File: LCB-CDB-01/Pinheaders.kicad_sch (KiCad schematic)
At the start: 4 parts, among them J60 Conn_02x30_Row_Letter_Last, J61 Conn_02x30_Row_Letter_Last, J62 Conn_02x30_Row_Letter_Last, J63 Conn_02x30_Row_Letter_Last

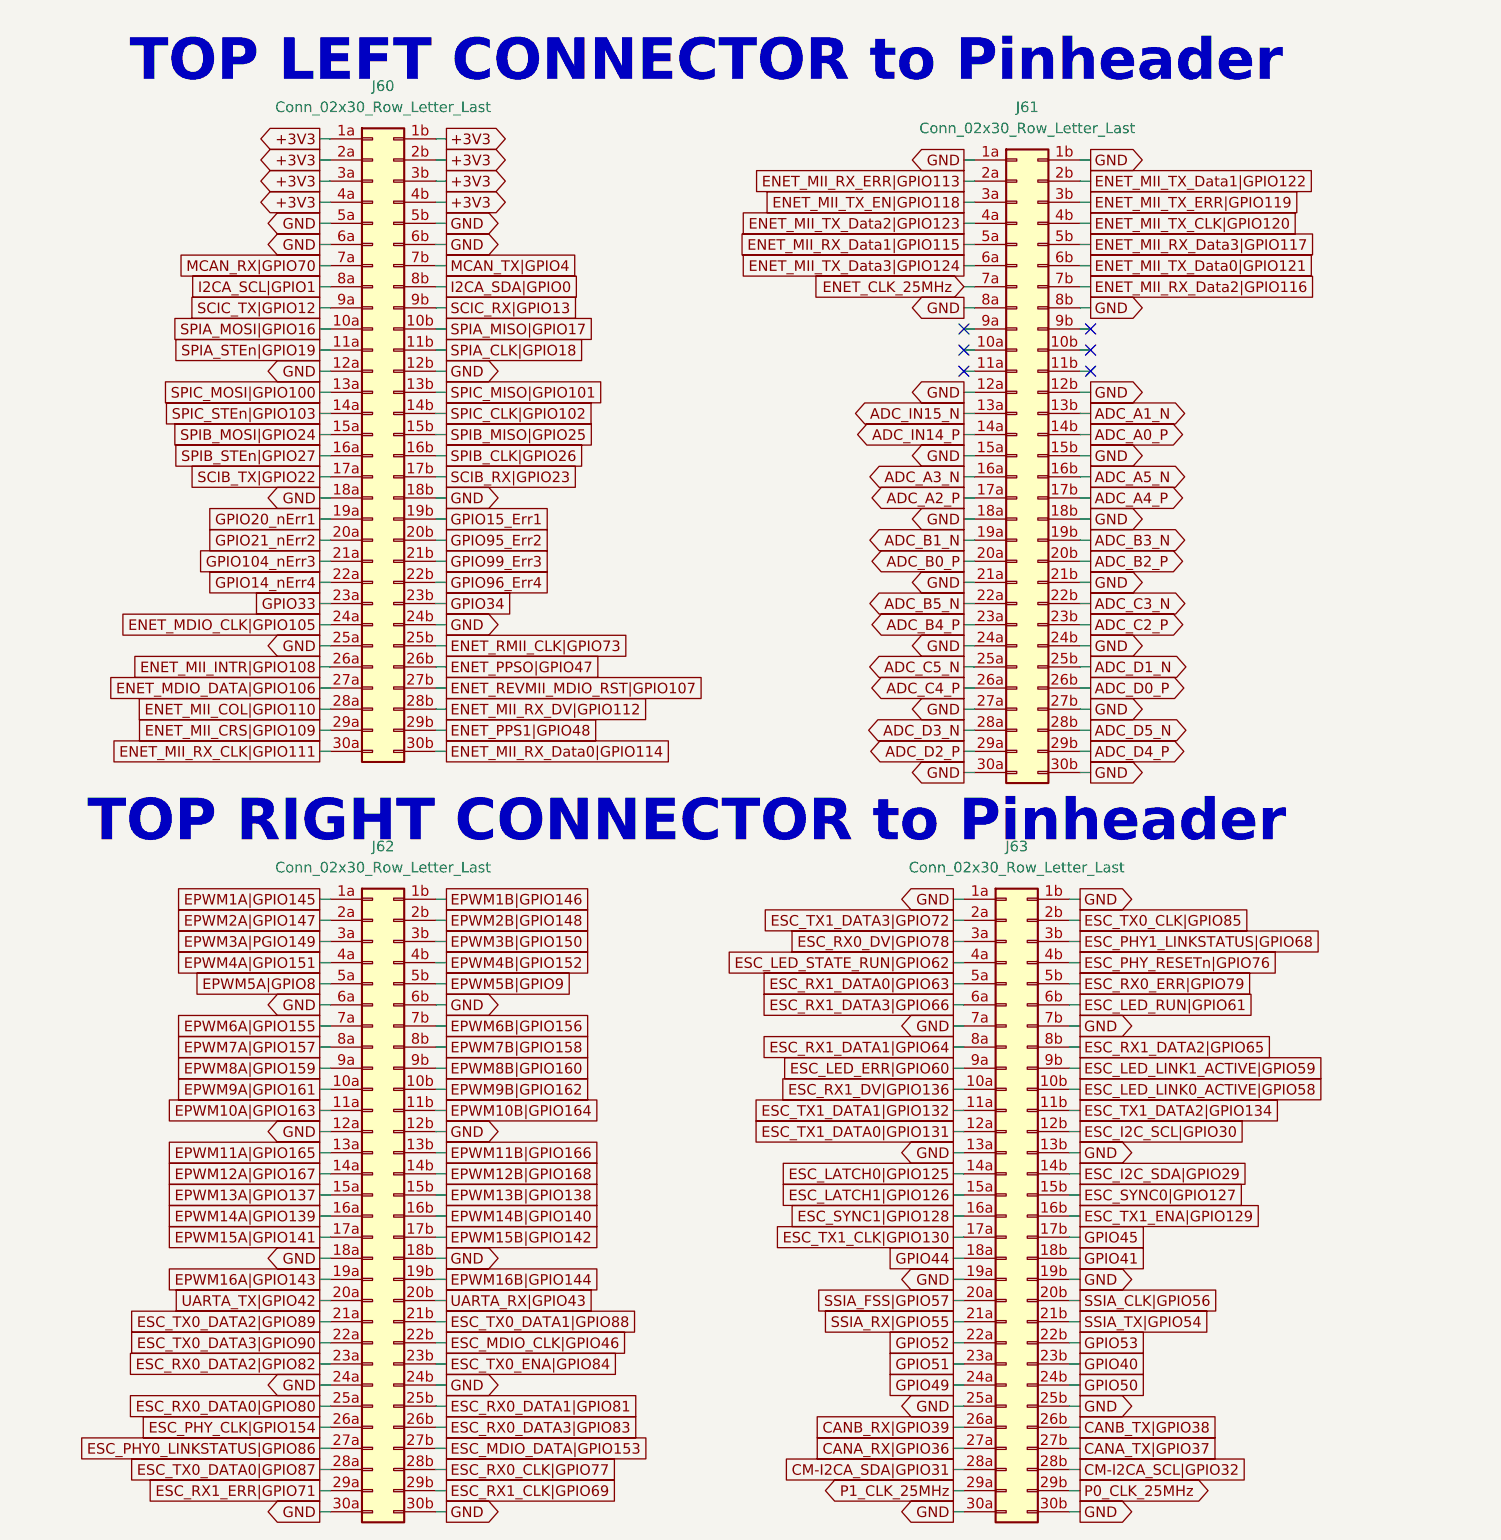
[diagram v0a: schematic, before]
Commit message: update some Rs and Cs names and values, as they can be separate values in KiCad7
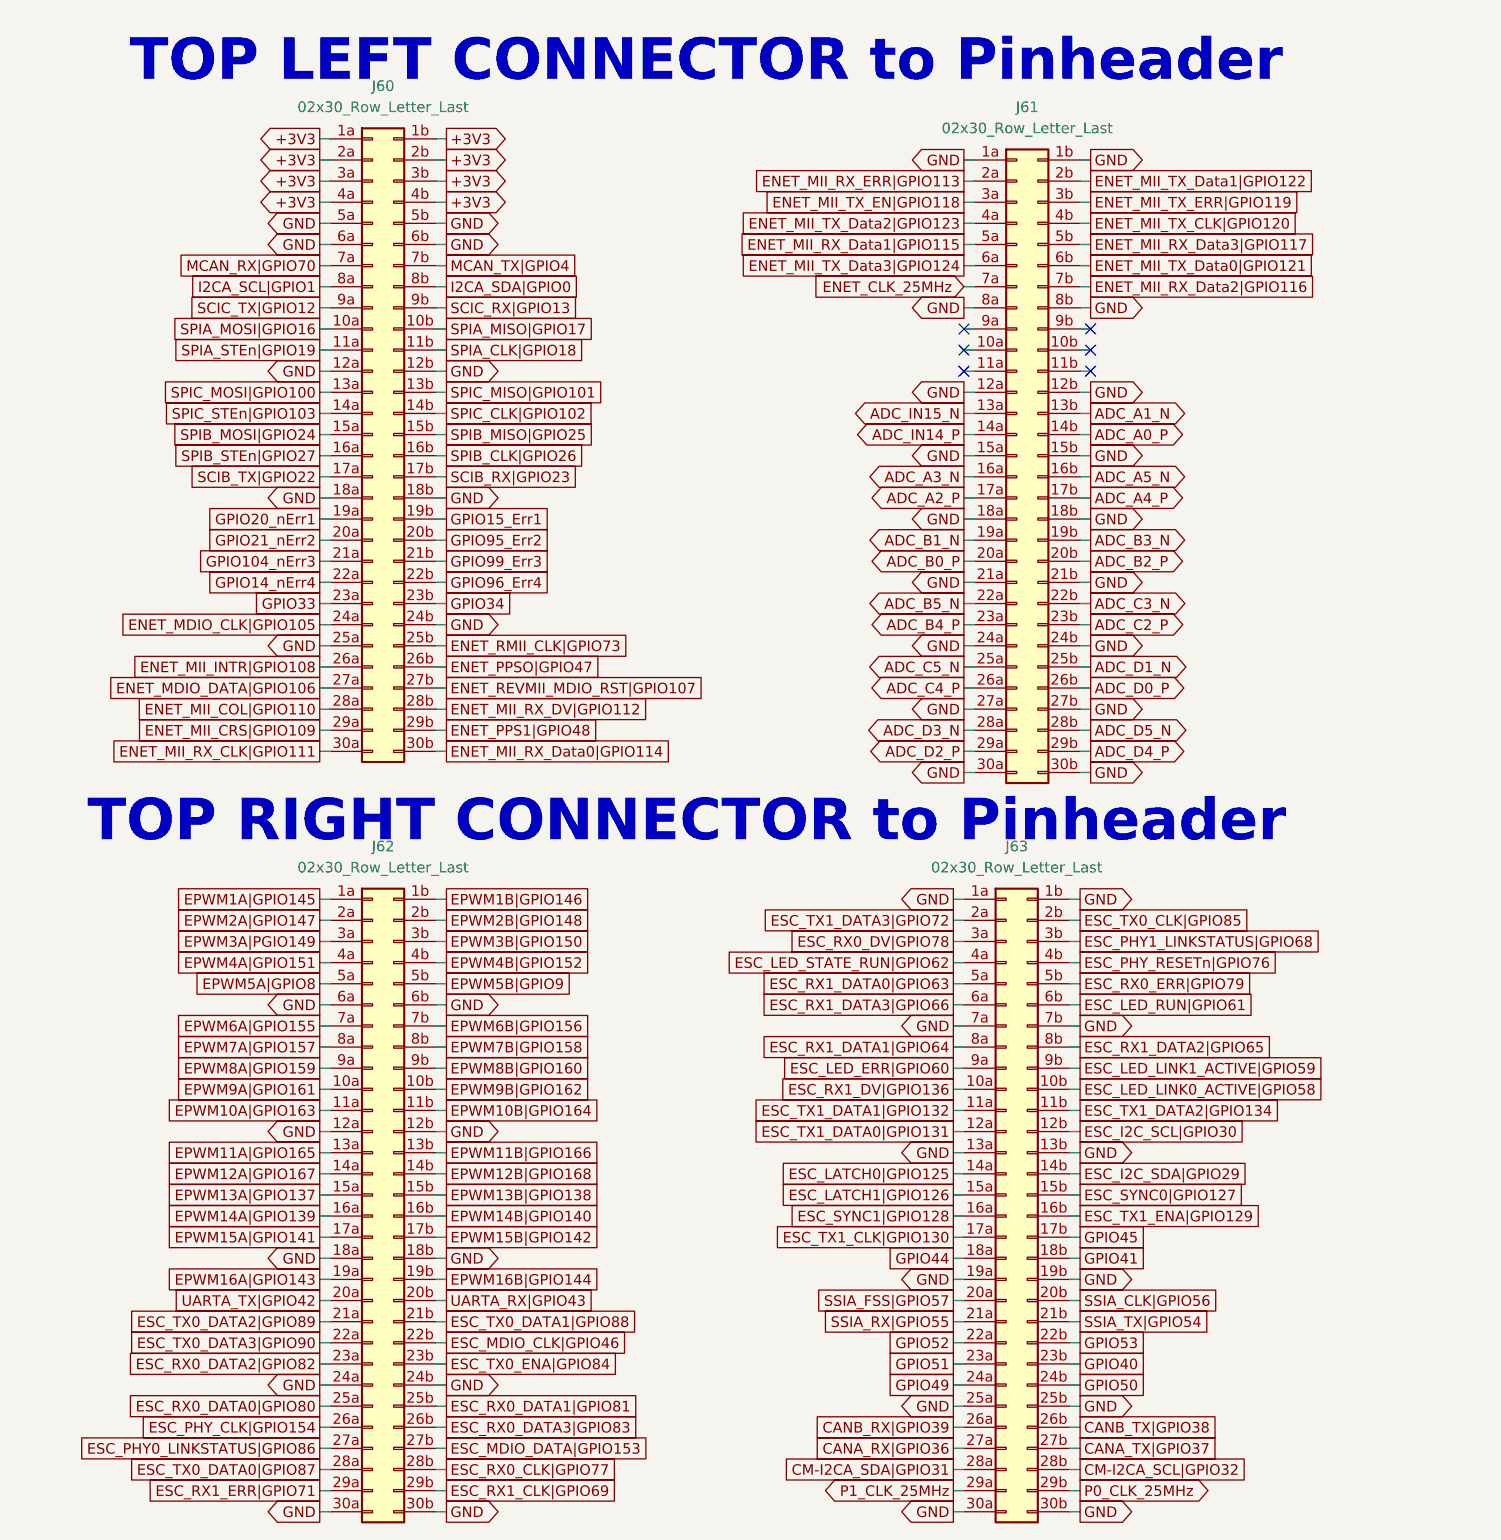
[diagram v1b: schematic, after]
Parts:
- J60, J61, J62, J63: value Conn_02x30_Row_Letter_Last -> 02x30_Row_Letter_Last
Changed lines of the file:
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@@
       (effects (font (size 1.27 1.27)))
     )
-    (property "Value" "Conn_02x30_Row_Letter_Last" (at 50.8 22.86 0)
+    (property "Value" "02x30_Row_Letter_Last" (at 50.8 22.86 0)
       (effects (font (size 1.27 1.27)))
     )
@@
       (effects (font (size 1.27 1.27)))
     )
-    (property "Value" "Conn_02x30_Row_Letter_Last" (at 50.8 114.3 0)
+    (property "Value" "02x30_Row_Letter_Last" (at 50.8 114.3 0)
       (effects (font (size 1.27 1.27)))
     )
@@
       (effects (font (size 1.27 1.27)))
     )
-    (property "Value" "Conn_02x30_Row_Letter_Last" (at 128.27 25.4 0)
+    (property "Value" "02x30_Row_Letter_Last" (at 128.27 25.4 0)
       (effects (font (size 1.27 1.27)))
     )
@@
       (effects (font (size 1.27 1.27)))
     )
-    (property "Value" "Conn_02x30_Row_Letter_Last" (at 127 114.3 0)
-      (effects (font (size 1.27 1.27)))
-    )
+    (property "Value" "02x30_Row_Letter_Last" (at 127 114.3 0)
+      (effects (font (size 1.27 1.27)))
+    )

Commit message: bump version to 1.1.0
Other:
- title: LCB-CBD-001: Dock -> LCB-CBD-01: Dock
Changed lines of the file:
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@@
   (paper "A4")
   (title_block
-    (title "LCB-CBD-001: Dock")
-    (date "2022-08-12")
-    (rev "0.1")
+    (title "LCB-CBD-01: Dock")
+    (date "2023-04-13")
+    (rev "1.1.0")
     (company "PADERBORN UNIVERSITY DEPARTMENT OF POWER ELECTRONICS AND ELECTRICAL DRIVES")
   )

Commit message: update symbols without simulation models
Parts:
- J60, J61, J62, J63: Mouser No. 649-77313-118-60LF -> (none)
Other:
- title: LCB-CBD-01: Dock -> LCB-CDB-01: Dock Board
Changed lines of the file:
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@@
 	(paper "A4")
 	(title_block
-		(title "LCB-CBD-01: Dock")
-		(date "2024-06-25")
+		(title "LCB-CDB-01: Dock Board")
+		(date "2024-07-16")
 		(rev "1.2.0")
 		(company "PADERBORN UNIVERSITY DEPARTMENT OF POWER ELECTRONICS AND ELECTRICAL DRIVES")
@@
 			)
 		)
-		(property "Mouser No." " 649-77313-118-60LF"
-			(at 41.91 7.62 0)
-			(effects
-				(font
-					(size 1.27 1.27)
-				)
-				(hide yes)
-			)
-		)
 		(property "mouser#" "649-77313-118-60LF"
 			(at 41.91 7.62 0)
@@
 			)
 		)
-		(property "Mouser No." " 649-77313-118-60LF"
-			(at 41.91 99.06 0)
-			(effects
-				(font
-					(size 1.27 1.27)
-				)
-				(hide yes)
-			)
-		)
 		(property "mouser#" "649-77313-118-60LF"
 			(at 41.91 99.06 0)
@@
 			)
 		)
-		(property "Mouser No." " 649-77313-118-60LF"
-			(at 119.38 10.16 0)
-			(effects
-				(font
-					(size 1.27 1.27)
-				)
-				(hide yes)
-			)
-		)
 		(property "mouser#" "649-77313-118-60LF"
 			(at 119.38 10.16 0)
@@
 			(effects
 				(font
-					(size 1.27 1.27)
-				)
-				(hide yes)
-			)
-		)
-		(property "Mouser No." " 649-77313-118-60LF"
-			(at 118.11 99.06 0)
-			(effects
-				(font
